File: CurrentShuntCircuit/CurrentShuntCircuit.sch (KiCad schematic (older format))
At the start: 45 parts, among them J1 Connection, J2 Connection, J3 Debug/UPDI, J4 ScrewTerminal, J5 Screw_Terminal_01x04, J6 ScrewTerminal, U1 VO1400AEF, U2 ATtiny1614-SS, U3 INA228, U4 ADM2483xRW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

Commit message: PCB layout
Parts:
- C11: value 47uF -> 47µF ±10% 16V Ceramic X5R
- J5: LCSCStockCode (none) -> C395880
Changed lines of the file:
@@
 F 1 "400V 1A 1.3V @ 1A 150ns SMA" H 10145 2475 50  0000 C CNN
 F 2 "Diode_SMD:D_SMA" H 9640 2355 50  0001 C CNN
-F 3 "" H 9640 2355 50  0001 C CNN
-F 4 "" H 9640 2355 50  0001 C CNN "JLC"
-F 5 "C85103" H 9640 2355 50  0001 C CNN "LCSCStockCode"
-F 6 "RS1G-13-F" H 9640 2355 50  0001 C CNN "PartNumber"
+F 3 "https://datasheet.lcsc.com/szlcsc/1810170425_Diodes-Incorporated-RS1G-13-F_C85103.pdf" H 9640 2355 50  0001 C CNN
+F 4 "C85103" H 9640 2355 50  0001 C CNN "LCSCStockCode"
+F 5 "RS1G-13-F" H 9640 2355 50  0001 C CNN "PartNumber"
 	1    9640 2355
 	1    0    0    -1
@@
 P 10850 2770
 F 0 "C11" H 10965 2816 50  0000 L CNN
-F 1 "47uF" H 10965 2725 50  0000 L CNN
+F 1 "47µF ±10% 16V Ceramic X5R" V 10595 2540 50  0000 L CNN
 F 2 "Capacitor_SMD:C_1210_3225Metric" H 10888 2620 50  0001 C CNN
-F 3 "~" H 10850 2770 50  0001 C CNN
-F 4 "" H 10850 2770 50  0001 C CNN "JLC"
-F 5 "GRM32ER61C476KE15L" H 10850 2770 50  0001 C CNN "PartNumber"
-F 6 "C77101" H 10850 2770 50  0001 C CNN "LCSCStockCode"
+F 3 "https://search.murata.co.jp/Ceramy/image/img/A01X/G101/ENG/GRM32ER61C476KE15-01.pdf" H 10850 2770 50  0001 C CNN
+F 4 "GRM32ER61C476KE15L" H 10850 2770 50  0001 C CNN "PartNumber"
+F 5 "C77101" H 10850 2770 50  0001 C CNN "LCSCStockCode"
 	1    10850 2770
 	-1   0    0    1
@@
 F 2 "CurrentShuntCircuit:Terminal-Block_3.81_4P_LCSC_C395880" H 9570 5370 50  0001 C CNN
 F 3 "~" H 9570 5370 50  0001 C CNN
+F 4 "C395880" H 9570 5370 50  0001 C CNN "LCSCStockCode"
 	1    9570 5370
 	1    0    0    -1

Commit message: Updated
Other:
- note removed: "SHUNTS\n\nhttps://shunts.com/\nRIEDON SHUNTS, 50mV and 100mV output\nhttps://shunts.com/collections/shunts/products/mka?variant=35787073126552\n\nMKA-75, Operating current 50A\nMKB-200, operating current 133A\nMKB-300, operating current 200A\nMKB-500, operating current 333A\n\nShunts should be placed on side, longest side horizontal\nMKA, 50.8mm wide, 31.8mm high\nMKB, 82.6mm wide, 44.5mm high\n"
- moved on the sheet: C2, C4, D2, D3, J6, R10, R11, R14, R15, R8, R9, U1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

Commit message: First Gerbers
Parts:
- added R16: 470R, Resistor_SMD:R_0805_2012Metric, symbol Device:R
- R12: LCSCStockCode (none) -> C17437; PartNumber (none) -> 0805W8F1200T5E
- U1: value VO1400AEF -> TLP172GM; footprint Package_SO:SO-4_4.4x4.3mm_P2.54mm -> Package_SO:SO-4_4.4x3.6mm_P2.54mm; LCSCStockCode C142551 -> C261926; PartNumber VO1400AEF -> TLP172GM
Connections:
- wire segments 119 -> 120
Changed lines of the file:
@@
 P 4980 5005
 F 0 "U1" H 4980 4688 50  0000 C CNN
-F 1 "VO1400AEF" H 4980 4779 50  0000 C CNN
-F 2 "Package_SO:SO-4_4.4x4.3mm_P2.54mm" H 4780 4805 50  0001 L CIN
-F 3 "https://datasheet.lcsc.com/szlcsc/Vishay-Intertech-VO1400AEFTR_C142551.pdf" H 4980 5005 50  0001 L CNN
-F 4 "VO1400AEF" H 4980 5005 50  0001 C CNN "PartNumber"
-F 5 "C142551" H 4980 5005 50  0001 C CNN "LCSCStockCode"
+F 1 "TLP172GM" H 4980 4779 50  0000 C CNN
+F 2 "Package_SO:SO-4_4.4x3.6mm_P2.54mm" H 4780 4805 50  0001 L CIN
+F 3 "https://datasheet.lcsc.com/szlcsc/TOSHIBA-TLP172GM-TPL-E-O_C261926.pdf" H 4980 5005 50  0001 L CNN
+F 4 "TLP172GM" H 4980 5005 50  0001 C CNN "PartNumber"
+F 5 "C261926" H 4980 5005 50  0001 C CNN "LCSCStockCode"
 	1    4980 5005
 	1    0    0    -1
@@
 	1    0    0    -1
 $EndComp
-Text GLabel 4105 5990 2    59   Input ~ 0
+Text GLabel 4770 5990 2    59   Input ~ 0
 RESET
 Text GLabel 2825 4535 2    59   Input ~ 0
@@
 F 2 "Resistor_SMD:R_0805_2012Metric" V 9165 5520 50  0001 C CNN
 F 3 "~" H 9235 5520 50  0001 C CNN
-F 4 "" H 9235 5520 50  0001 C CNN "LCSCStockCode"
-F 5 "" H 9235 5520 50  0001 C CNN "PartNumber"
+F 4 "C17437" H 9235 5520 50  0001 C CNN "LCSCStockCode"
+F 5 "0805W8F1200T5E" H 9235 5520 50  0001 C CNN "PartNumber"
 	1    9235 5520
 	-1   0    0    1
@@
 Text GLabel 4105 6590 2    59   Input ~ 0
 PA5
+$Comp
+L Device:R R16
+U 1 1 603AA795
+P 4620 5990
+F 0 "R16" H 4425 5995 50  0000 L CNN
+F 1 "470R" H 4375 5930 50  0000 L CNN
+F 2 "Resistor_SMD:R_0805_2012Metric" V 4550 5990 50  0001 C CNN
+F 3 "~" H 4620 5990 50  0001 C CNN
+F 4 "C17710" H 4620 5990 50  0001 C CNN "LCSCStockCode"
+F 5 "0805W8F4700T5E" H 4620 5990 50  0001 C CNN "PartNumber"
+	1    4620 5990
+	0    -1   -1   0
+$EndComp
+Wire Wire Line
+	4105 5990 4470 5990
 $EndSCHEMATC

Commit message: Updated Gerber
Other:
- note added: "Note 100V caps on input"
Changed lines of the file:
@@
 Wire Wire Line
 	4105 5990 4470 5990
+Text Notes 5940 2425 0    47   ~ 0
+Note 100V caps on input
 $EndSCHEMATC

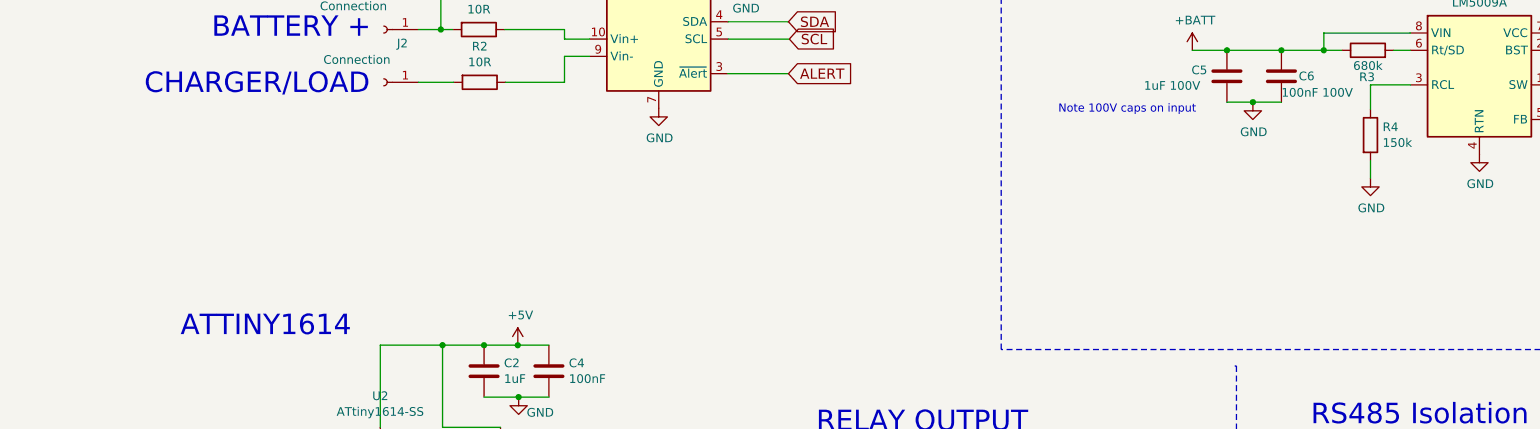
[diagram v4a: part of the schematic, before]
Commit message: Tweak of traces on PCB, improve silkscreen layout
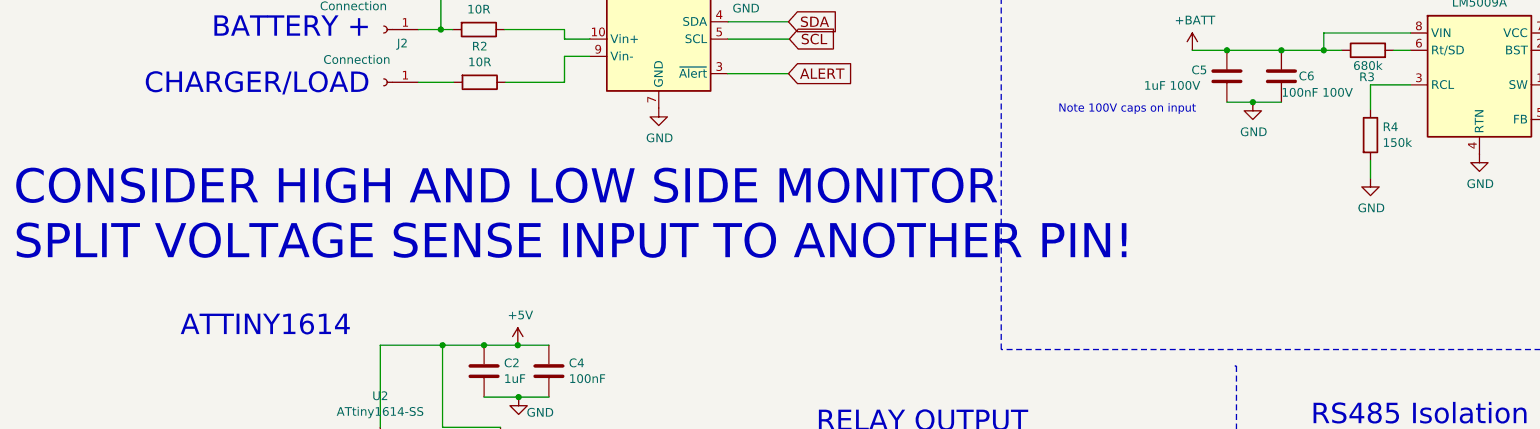
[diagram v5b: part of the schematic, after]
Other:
- note added: "CONSIDER HIGH AND LOW SIDE MONITOR\nSPLIT VOLTAGE SENSE INPUT TO ANOTHER PIN!"
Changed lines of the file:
@@
 Text Notes 5940 2425 0    47   ~ 0
 Note 100V caps on input
+Text Notes -100 3285 0    197  ~ 0
+CONSIDER HIGH AND LOW SIDE MONITOR\nSPLIT VOLTAGE SENSE INPUT TO ANOTHER PIN!
 $EndSCHEMATC

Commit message: Label TXRX
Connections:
- net labels added: A, B, VDD2
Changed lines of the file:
@@
 Text Notes -100 3285 0    197  ~ 0
 CONSIDER HIGH AND LOW SIDE MONITOR\nSPLIT VOLTAGE SENSE INPUT TO ANOTHER PIN!
+Text GLabel 9370 4985 2    50   Input ~ 0
+VDD2
+Text GLabel 9145 5330 1    50   Input ~ 0
+A
+Text GLabel 9075 5700 2    50   Input ~ 0
+B
 $EndSCHEMATC

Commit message: Tidy up tracks and positions - split VBUS into separate pin
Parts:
- added C14: 100nF 100V, Capacitor_SMD:C_0805_2012Metric, symbol Device:C
- J4: value ScrewTerminal -> Screw_Terminal_01x04; footprint CurrentShuntCircuit:Terminal-Block_3.81_2P-LCSC_C395878 -> CurrentShuntCircuit:Terminal-Block_3.81_4P_LCSC_C395880; symbol Connector:Screw_Terminal_01x02 -> Connector:Screw_Terminal_01x04; LCSCStockCode C395878 -> C395880
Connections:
- net labels added: BUSVOLTAGE
- wire segments 120 -> 124
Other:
- note removed: "CONSIDER HIGH AND LOW SIDE MONITOR\nSPLIT VOLTAGE SENSE INPUT TO ANOTHER PIN!"
- moved on the sheet: F1
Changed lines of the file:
@@
 	2445 2240 2240 2240
 Wire Wire Line
-	2740 1935 3085 1935
+	2740 1935 2840 1935
 Wire Wire Line
 	3085 1935 3085 1990
@@
 	3085 2090 3085 2240
 Wire Wire Line
-	3085 2240 2745 2240
+	3085 2240 2840 2240
 Text Notes 675  1355 0    50   ~ 0
 VIN- = Negative input to the device. \nhigh-side:connect to load side of sense resistor. \n\nVIN+ = Positive input to the device. \nhigh-side: connect to power supply side of sense resistor\n
@@
 Wire Wire Line
 	4030 1640 4030 1690
-Wire Wire Line
-	2240 1935 2370 1935
-Wire Wire Line
-	2370 1935 2370 1590
-Wire Wire Line
-	2370 1590 3230 1590
-Connection ~ 2370 1935
-Wire Wire Line
-	2370 1935 2440 1935
 $Comp
 L Relay_SolidState:ASSR-1218 U1
@@
 $EndComp
 $Comp
-L Connector:Screw_Terminal_01x02 J4
+L Connector:Screw_Terminal_01x04 J4
 U 1 1 60366551
-P 6790 1265
-F 0 "J4" H 6790 1070 50  0000 C CNN
-F 1 "ScrewTerminal" H 7270 1205 50  0000 C CNN
-F 2 "CurrentShuntCircuit:Terminal-Block_3.81_2P-LCSC_C395878" H 6790 1265 50  0001 C CNN
-F 3 "https://datasheet.lcsc.com/szlcsc/1912111437_DIBO-DB125-3-81-2P-GN_C395878.pdf" H 6790 1265 50  0001 C CNN
-F 4 "C395878" H 6790 1265 50  0001 C CNN "LCSCStockCode"
-	1    6790 1265
+P 6620 1300
+F 0 "J4" H 6620 1105 50  0000 C CNN
+F 1 "Screw_Terminal_01x04" H 7100 1240 50  0000 C CNN
+F 2 "CurrentShuntCircuit:Terminal-Block_3.81_4P_LCSC_C395880" H 6620 1300 50  0001 C CNN
+F 3 "" H 6620 1300 50  0001 C CNN
+F 4 "C395880" H 6620 1300 50  0001 C CNN "LCSCStockCode"
+	1    6620 1300
 	-1   0    0    1
 $EndComp
@@
 L power:GND #PWR08
 U 1 1 6036808B
-P 6990 1265
-F 0 "#PWR08" H 6990 1015 50  0001 C CNN
-F 1 "GND" H 6995 1092 50  0000 C CNN
-F 2 "" H 6990 1265 50  0001 C CNN
-F 3 "" H 6990 1265 50  0001 C CNN
-	1    6990 1265
+P 6820 1400
+F 0 "#PWR08" H 6820 1150 50  0001 C CNN
+F 1 "GND" H 6825 1227 50  0000 C CNN
+F 2 "" H 6820 1400 50  0001 C CNN
+F 3 "" H 6820 1400 50  0001 C CNN
+	1    6820 1400
 	1    0    0    -1
 $EndComp
@@
 L power:+BATT #PWR09
 U 1 1 60368C54
-P 7590 1165
-F 0 "#PWR09" H 7590 1015 50  0001 C CNN
-F 1 "+BATT" H 7605 1338 50  0000 C CNN
-F 2 "" H 7590 1165 50  0001 C CNN
-F 3 "" H 7590 1165 50  0001 C CNN
-	1    7590 1165
+P 7420 1100
+F 0 "#PWR09" H 7420 950 50  0001 C CNN
+F 1 "+BATT" H 7565 1135 50  0000 C CNN
+F 2 "" H 7420 1100 50  0001 C CNN
+F 3 "" H 7420 1100 50  0001 C CNN
+	1    7420 1100
 	1    0    0    -1
 $EndComp
@@
 L Device:Polyfuse F1
 U 1 1 6036C4B0
-P 7290 1165
-F 0 "F1" V 7065 1165 50  0000 C CNN
-F 1 "Through Hole PTC" V 7156 1165 50  0000 C CNN
-F 2 "Fuse:Fuse_BelFuse_0ZRE0005FF_L8.3mm_W3.8mm" H 7340 965 50  0001 L CNN
-F 3 "https://datasheet.lcsc.com/szlcsc/1912111437_Jinrui-Electronic-Materials-Co-JK250-120U_C369130.pdf" H 7290 1165 50  0001 C CNN
-F 4 "C2680606" H 7290 1165 50  0001 C CNN "LCSCStockCode"
-F 5 "JK250-100U" H 7290 1165 50  0001 C CNN "PartNumber"
-	1    7290 1165
+P 7120 1100
+F 0 "F1" V 6895 1100 50  0000 C CNN
+F 1 "Through Hole PTC" V 6986 1100 50  0000 C CNN
+F 2 "Fuse:Fuse_BelFuse_0ZRE0005FF_L8.3mm_W3.8mm" H 7170 900 50  0001 L CNN
+F 3 "https://datasheet.lcsc.com/szlcsc/1912111437_Jinrui-Electronic-Materials-Co-JK250-120U_C369130.pdf" H 7120 1100 50  0001 C CNN
+F 4 "C2680606" H 7120 1100 50  0001 C CNN "LCSCStockCode"
+F 5 "JK250-100U" H 7120 1100 50  0001 C CNN "PartNumber"
+	1    7120 1100
 	0    1    1    0
 $EndComp
 Wire Wire Line
-	7440 1165 7590 1165
-Wire Wire Line
-	7140 1165 6990 1165
+	7270 1100 7420 1100
+Wire Wire Line
+	6970 1100 6820 1100
 $Comp
 L power:+BATT #PWR010
@@
 Text Notes 5940 2425 0    47   ~ 0
 Note 100V caps on input
-Text Notes -100 3285 0    197  ~ 0
-CONSIDER HIGH AND LOW SIDE MONITOR\nSPLIT VOLTAGE SENSE INPUT TO ANOTHER PIN!
 Text GLabel 9370 4985 2    50   Input ~ 0
 VDD2
@@
 Text GLabel 9075 5700 2    50   Input ~ 0
 B
+$Comp
+L Device:C C14
+U 1 1 605A1F4C
+P 2840 2085
+F 0 "C14" H 2940 2085 50  0000 L CNN
+F 1 "100nF 100V" H 2840 1990 50  0000 L CNN
+F 2 "Capacitor_SMD:C_0805_2012Metric" H 2878 1935 50  0001 C CNN
+F 3 "https://datasheet.lcsc.com/szlcsc/2008131833_KEMET-C0805C104K1RECAUTO_C696367.pdf" H 2840 2085 50  0001 C CNN
+F 4 "" H 2840 2085 50  0001 C CNN "JLC"
+F 5 "C0805C104K1RECAUTO" H 2840 2085 50  0001 C CNN "PartNumber"
+F 6 "C696367" H 2840 2085 50  0001 C CNN "LCSCStockCode"
+	1    2840 2085
+	1    0    0    -1
+$EndComp
+Connection ~ 2840 1935
+Wire Wire Line
+	2840 1935 3085 1935
+Wire Wire Line
+	2840 2240 2840 2235
+Connection ~ 2840 2240
+Wire Wire Line
+	2840 2240 2745 2240
+Text Notes 2485 2405 0    47   ~ 0
+Note 100V caps on input
+Text GLabel 3080 1590 1    59   Input ~ 0
+BUSVOLTAGE
+Wire Wire Line
+	2240 1935 2440 1935
+Wire Wire Line
+	3080 1590 3230 1590
+Wire Wire Line
+	6820 1300 6890 1300
+Wire Wire Line
+	6890 1300 6890 1400
+Wire Wire Line
+	6890 1400 6820 1400
+Connection ~ 6820 1400
+Text GLabel 6820 1200 2    59   Input ~ 0
+BUSVOLTAGE
 $EndSCHEMATC

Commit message: Swap to use DIP switch for config selection
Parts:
- added SW1: SW_DIP_x02, CurrentShuntCircuit:XKBConnectivity_DSHP02TS-S_P1.27, symbol Switch:SW_DIP_x02
- J3: footprint Connector_PinHeader_2.54mm:PinHeader_1x12_P2.54mm_Vertical -> Connector_PinHeader_2.54mm:PinHeader_1x08_P2.54mm_Vertical; symbol Connector:Conn_01x12_Male -> Connector:Conn_01x08_Male; LCSCStockCode C50981 -> (none)
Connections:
- wire segments 124 -> 121
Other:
- moved on the sheet: R16
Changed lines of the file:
@@
 L power:+5V #PWR0102
 U 1 1 603FB280
-P 4105 5890
-F 0 "#PWR0102" H 4105 5740 50  0001 C CNN
-F 1 "+5V" H 4120 6063 50  0000 C CNN
-F 2 "" H 4105 5890 50  0001 C CNN
-F 3 "" H 4105 5890 50  0001 C CNN
-	1    4105 5890
-	1    0    0    -1
-$EndComp
-Text GLabel 4770 5990 2    59   Input ~ 0
+P 4125 6075
+F 0 "#PWR0102" H 4125 5925 50  0001 C CNN
+F 1 "+5V" H 4140 6248 50  0000 C CNN
+F 2 "" H 4125 6075 50  0001 C CNN
+F 3 "" H 4125 6075 50  0001 C CNN
+	1    4125 6075
+	1    0    0    -1
+$EndComp
+Text GLabel 4790 6175 2    59   Input ~ 0
 RESET
 Text GLabel 2825 4535 2    59   Input ~ 0
@@
 Text GLabel 2620 4935 2    59   Input ~ 0
 PA4
-Text GLabel 4105 6990 2    59   Input ~ 0
+Text GLabel 5535 6700 0    59   Input ~ 0
 PA4
 $Comp
-L Connector:Conn_01x12_Male J3
+L Connector:Conn_01x08_Male J3
 U 1 1 604C0657
-P 3905 6390
-F 0 "J3" H 3790 6700 50  0000 C CNN
-F 1 "Debug/UPDI" V 3755 6230 50  0000 C CNN
-F 2 "Connector_PinHeader_2.54mm:PinHeader_1x12_P2.54mm_Vertical" H 3905 6390 50  0001 C CNN
-F 3 "~" H 3905 6390 50  0001 C CNN
-F 4 "C50981" H 3905 6390 50  0001 C CNN "LCSCStockCode"
-F 5 "" H 3905 6390 50  0001 C CNN "PartNumber"
-	1    3905 6390
-	1    0    0    -1
-$EndComp
-Text GLabel 4105 6390 2    59   Input ~ 0
+P 3925 6375
+F 0 "J3" H 4100 5825 50  0000 C CNN
+F 1 "Debug/UPDI" V 3795 6350 50  0000 C CNN
+F 2 "Connector_PinHeader_2.54mm:PinHeader_1x08_P2.54mm_Vertical" H 3925 6375 50  0001 C CNN
+F 3 "~" H 3925 6375 50  0001 C CNN
+F 4 "" H 3925 6375 50  0001 C CNN "LCSCStockCode"
+F 5 "" H 3925 6375 50  0001 C CNN "PartNumber"
+	1    3925 6375
+	1    0    0    -1
+$EndComp
+Text GLabel 4125 6575 2    59   Input ~ 0
 TXD
-Text GLabel 4105 6490 2    59   Input ~ 0
+Text GLabel 4125 6675 2    59   Input ~ 0
 RXD
 $Comp
 L power:GND #PWR026
 U 1 1 604C270C
-P 4450 6090
-F 0 "#PWR026" H 4450 5840 50  0001 C CNN
-F 1 "GND" H 4455 5917 50  0000 C CNN
-F 2 "" H 4450 6090 50  0001 C CNN
-F 3 "" H 4450 6090 50  0001 C CNN
-	1    4450 6090
-	1    0    0    -1
-$EndComp
-Text GLabel 4105 6190 2    59   Input ~ 0
+P 4470 6275
+F 0 "#PWR026" H 4470 6025 50  0001 C CNN
+F 1 "GND" H 4475 6102 50  0000 C CNN
+F 2 "" H 4470 6275 50  0001 C CNN
+F 3 "" H 4470 6275 50  0001 C CNN
+	1    4470 6275
+	1    0    0    -1
+$EndComp
+Text GLabel 4125 6375 2    59   Input ~ 0
 SCL
-Text GLabel 4105 6290 2    59   Input ~ 0
+Text GLabel 4125 6475 2    59   Input ~ 0
 SDA
 Text Notes 7400 4235 0    118  ~ 0
@@
 Text Notes 4540 4275 0    118  ~ 0
 RELAY OUTPUT
-Wire Wire Line
-	4105 6090 4370 6090
 Wire Notes Line
 	11115 3785 5610 3785
@@
 Wire Notes Line
 	6970 3880 6970 6430
-Text Notes 4350 7015 0    50   ~ 0
+Text Notes 5130 6895 0    50   ~ 0
 Modbus Address
-Text Notes 4450 6870 0    50   ~ 0
+Text Notes 5150 6510 0    50   ~ 0
 Baud Rate
-Text GLabel 4105 6790 2    59   Input ~ 0
+Text GLabel 5535 6600 0    59   Input ~ 0
 PA3
-Text Notes 3920 6090 1    50   ~ 0
+Text Notes 3925 6265 1    50   ~ 0
 UPDI
-Wire Wire Line
-	4105 6690 4370 6690
-Wire Wire Line
-	4370 6690 4370 6090
-Connection ~ 4370 6090
-Wire Wire Line
-	4370 6090 4450 6090
-Wire Wire Line
-	4105 6890 4370 6890
-Wire Wire Line
-	4370 6890 4370 6690
-Connection ~ 4370 6690
-Text GLabel 4105 6590 2    59   Input ~ 0
+Text GLabel 4125 6775 2    59   Input ~ 0
 PA5
 $Comp
 L Device:R R16
 U 1 1 603AA795
-P 4620 5990
-F 0 "R16" H 4425 5995 50  0000 L CNN
-F 1 "470R" H 4375 5930 50  0000 L CNN
-F 2 "Resistor_SMD:R_0805_2012Metric" V 4550 5990 50  0001 C CNN
-F 3 "~" H 4620 5990 50  0001 C CNN
-F 4 "C17710" H 4620 5990 50  0001 C CNN "LCSCStockCode"
-F 5 "0805W8F4700T5E" H 4620 5990 50  0001 C CNN "PartNumber"
-	1    4620 5990
+P 4640 6175
+F 0 "R16" H 4445 6180 50  0000 L CNN
+F 1 "470R" H 4395 6115 50  0000 L CNN
+F 2 "Resistor_SMD:R_0805_2012Metric" V 4570 6175 50  0001 C CNN
+F 3 "~" H 4640 6175 50  0001 C CNN
+F 4 "C17710" H 4640 6175 50  0001 C CNN "LCSCStockCode"
+F 5 "0805W8F4700T5E" H 4640 6175 50  0001 C CNN "PartNumber"
+	1    4640 6175
 	0    -1   -1   0
 $EndComp
 Wire Wire Line
-	4105 5990 4470 5990
+	4125 6175 4490 6175
 Text Notes 5940 2425 0    47   ~ 0
 Note 100V caps on input
@@
 Text GLabel 6820 1200 2    59   Input ~ 0
 BUSVOLTAGE
+$Comp
+L Switch:SW_DIP_x02 SW1
+U 1 1 60702D2D
+P 5835 6700
+F 0 "SW1" H 5835 7067 50  0000 C CNN
+F 1 "SW_DIP_x02" H 5835 6976 50  0000 C CNN
+F 2 "CurrentShuntCircuit:XKBConnectivity_DSHP02TS-S_P1.27" H 5835 6700 50  0001 C CNN
+F 3 "https://datasheet.lcsc.com/szlcsc/2002271742_XKB-Connectivity-DSHP02TS-S_C319052.pdf" H 5835 6700 50  0001 C CNN
+F 4 "C319052" H 5835 6700 50  0001 C CNN "LCSCStockCode"
+	1    5835 6700
+	1    0    0    -1
+$EndComp
+$Comp
+L power:GND #PWR0103
+U 1 1 6070355F
+P 6235 6700
+F 0 "#PWR0103" H 6235 6450 50  0001 C CNN
+F 1 "GND" H 6240 6527 50  0000 C CNN
+F 2 "" H 6235 6700 50  0001 C CNN
+F 3 "" H 6235 6700 50  0001 C CNN
+	1    6235 6700
+	1    0    0    -1
+$EndComp
+Wire Wire Line
+	6135 6600 6135 6700
+Wire Wire Line
+	6135 6700 6235 6700
+Connection ~ 6135 6700
+Wire Wire Line
+	4125 6275 4470 6275
 $EndSCHEMATC
